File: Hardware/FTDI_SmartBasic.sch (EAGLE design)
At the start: 28 parts, among them U1 FT232RLSSOP, U2 MIC5219 3.3V, U3 TS3USB221A

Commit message: Incorporate changes from review
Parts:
- LOGO2: value SFE_LOGO_NAME_FLAME.1_INCH -> SFE_LOGO_FLAME.2_INCH; device SparkFun-Aesthetics:SFE_LOGO_NAME_FLAME.1_INCH -> SparkFun-Aesthetics:SFE_LOGO_FLAME.2_INCH
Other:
- note added: "01"
- note added: "Mike Hord"
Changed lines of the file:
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@@
 <part name="U$1" library="SparkFun-Aesthetics" deviceset="SMART_BASIC_LOGO" device=""/>
 <part name="LOGO1" library="SparkFun-Aesthetics" deviceset="SFE_LOGO_NAME" device=".1_INCH"/>
-<part name="LOGO2" library="SparkFun-Aesthetics" deviceset="SFE_LOGO_NAME_FLAME" device=".1_INCH"/>
 <part name="LOGO3" library="SparkFun-Aesthetics" deviceset="OSHW-LOGO" device="S"/>
+<part name="LOGO2" library="SparkFun-Aesthetics" deviceset="SFE_LOGO_FLAME" device=".2_INCH" value="SFE_LOGO_FLAME.2_INCH"/>
 </parts>
 <sheets>
@@
 Pro Mini,
 LilyPad, etc.</text>
+<text x="167.64" y="7.62" size="3.81" layer="91" font="vector">Mike Hord</text>
+<text x="239.014" y="6.604" size="3.81" layer="91" font="vector">01</text>
 </plain>
 <instances>
@@
 <instance part="U$1" gate="G$1" x="215.9" y="38.1"/>
 <instance part="LOGO1" gate="G$1" x="87.63" y="3.048"/>
-<instance part="LOGO2" gate="G$1" x="88.9" y="2.54"/>
 <instance part="LOGO3" gate="G$1" x="76.2" y="12.7"/>
+<instance part="LOGO2" gate="G$1" x="132.08" y="22.86"/>
 </instances>
 <busses>

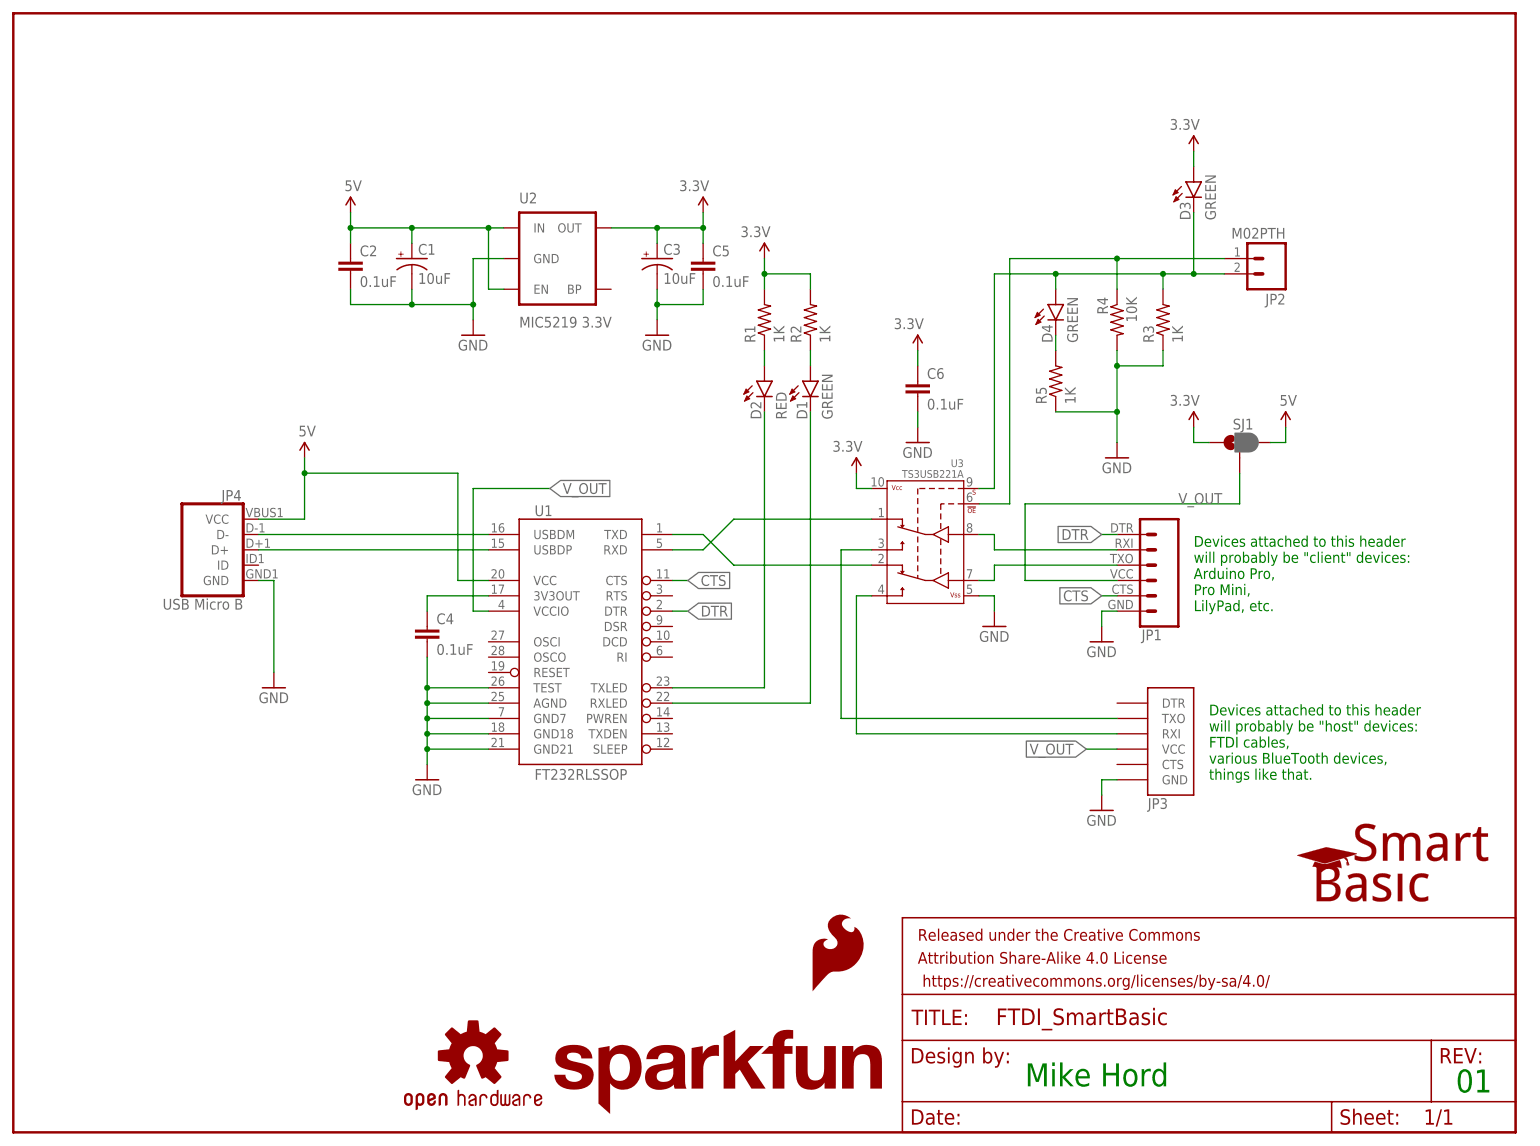
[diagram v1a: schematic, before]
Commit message: 2nd round protos - add vias to strain relief pads on connector - flip the client connector - remove the USB indicator LED and change other LED label - change silk from JP1 and JP3 to HOST and CLIENT
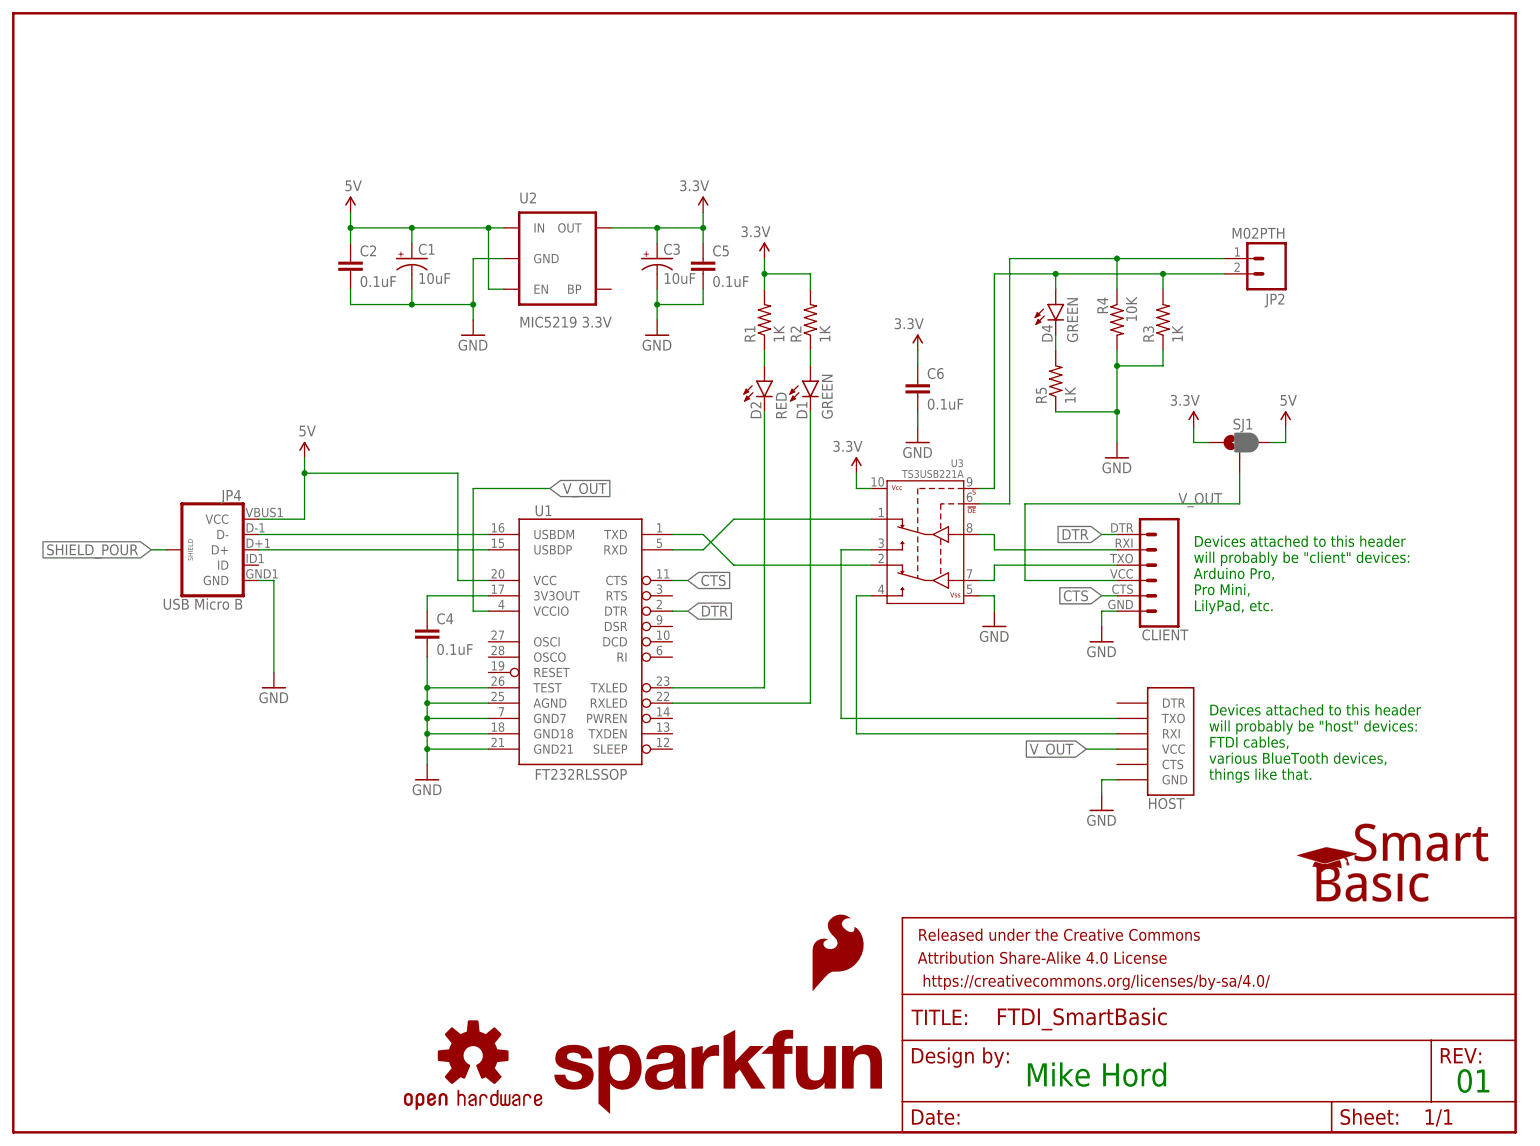
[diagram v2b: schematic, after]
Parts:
- removed D3: GREEN, SparkFun-LED:LED-GREEN0603
- renumbered JP1 to CLIENT, JP3 to HOST
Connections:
- new net SHIELD_POUR: JP4.SHIELD
- net 3.3V: no longer D3.A
- net SELECT: no longer D3.C
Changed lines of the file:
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@@
 <part name="GND1" library="SparkFun-Aesthetics" deviceset="GND" device=""/>
 <part name="SUPPLY4" library="SparkFun-Aesthetics" deviceset="5V" device=""/>
-<part name="JP1" library="SparkFun-Connectors" deviceset="FTDI_BASIC" device="PTH" value=""/>
+<part name="CLIENT" library="SparkFun-Connectors" deviceset="FTDI_BASIC" device="PTH" value=""/>
 <part name="R1" library="SparkFun-Resistors" deviceset="1KOHM1/10W1%(0603)" device="" value="1K"/>
 <part name="R2" library="SparkFun-Resistors" deviceset="1KOHM1/10W1%(0603)" device="" value="1K"/>
@@
 <part name="C3" library="SparkFun-Capacitors" deviceset="10UF-16V-10%(TANT)" device="" value="10uF"/>
 <part name="U3" library="SparkFun-AnalogIC" deviceset="TS3USB221A" device="" value="TS3USB221A"/>
-<part name="JP3" library="SparkFun-Connectors" deviceset="FTDI_DEVICE" device="" value=""/>
+<part name="HOST" library="SparkFun-Connectors" deviceset="FTDI_DEVICE" device="" value=""/>
 <part name="JP4" library="SparkFun-Connectors" deviceset="USB_MICROB_PLUG" device="CONN-11752" value="USB Micro B"/>
 <part name="SUPPLY6" library="SparkFun-Aesthetics" deviceset="3.3V" device=""/>
@@
 <part name="SUPPLY2" library="SparkFun-Aesthetics" deviceset="3.3V" device=""/>
 <part name="R3" library="SparkFun-Resistors" deviceset="1KOHM1/10W1%(0603)" device="" value="1K"/>
-<part name="D3" library="SparkFun-LED" deviceset="LED-GREEN" device="0603" value="GREEN"/>
-<part name="SUPPLY5" library="SparkFun-Aesthetics" deviceset="3.3V" device=""/>
 <part name="D4" library="SparkFun-LED" deviceset="LED-GREEN" device="0603" value="GREEN"/>
 <part name="R5" library="SparkFun-Resistors" deviceset="1KOHM1/10W1%(0603)" device="" value="1K"/>
@@
 <instance part="GND1" gate="1" x="43.18" y="73.66"/>
 <instance part="SUPPLY4" gate="G$1" x="48.26" y="111.76"/>
-<instance part="JP1" gate="G$1" x="187.96" y="93.98" smashed="yes" rot="R180">
+<instance part="CLIENT" gate="G$1" x="187.96" y="93.98" smashed="yes" rot="R180">
 <attribute name="VALUE" x="193.04" y="104.14" size="1.778" layer="96" rot="R180"/>
 <attribute name="NAME" x="186.944" y="81.534" size="1.778" layer="95"/>
@@
 <instance part="C3" gate="G$1" x="106.68" y="144.78"/>
 <instance part="U3" gate="G$1" x="157.48" y="88.9" rot="MR0"/>
-<instance part="JP3" gate="G$1" x="187.96" y="66.04" smashed="yes">
+<instance part="HOST" gate="G$1" x="187.96" y="66.04" smashed="yes">
 <attribute name="NAME" x="187.96" y="53.594" size="1.778" layer="95"/>
 <attribute name="VALUE" x="187.96" y="73.66" size="1.778" layer="96"/>
@@
 <instance part="SUPPLY2" gate="G$1" x="124.46" y="144.78" rot="MR0"/>
 <instance part="R3" gate="G$1" x="190.5" y="134.62" rot="R90"/>
-<instance part="D3" gate="G$1" x="195.58" y="157.48" smashed="yes">
-<attribute name="NAME" x="195.072" y="151.13" size="1.778" layer="95" rot="R90"/>
-<attribute name="VALUE" x="199.263" y="151.13" size="1.778" layer="96" rot="R90"/>
-</instance>
-<instance part="SUPPLY5" gate="G$1" x="195.58" y="162.56" rot="MR0"/>
 <instance part="D4" gate="G$1" x="172.72" y="137.16" smashed="yes">
 <attribute name="NAME" x="172.212" y="130.81" size="1.778" layer="95" rot="R90"/>
@@
 <pinref part="GND4" gate="1" pin="GND"/>
 <wire x1="180.34" y1="83.82" x2="180.34" y2="86.36" width="0.1524" layer="91"/>
-<pinref part="JP1" gate="G$1" pin="6"/>
+<pinref part="CLIENT" gate="G$1" pin="6"/>
 <wire x1="180.34" y1="86.36" x2="182.88" y2="86.36" width="0.1524" layer="91"/>
 </segment>
@@
 </segment>
 <segment>
-<pinref part="JP3" gate="G$1" pin="GND"/>
+<pinref part="HOST" gate="G$1" pin="GND"/>
 <pinref part="GND8" gate="1" pin="GND"/>
 <wire x1="182.88" y1="58.42" x2="180.34" y2="58.42" width="0.1524" layer="91"/>
@@
 </segment>
 <segment>
-<pinref part="D3" gate="G$1" pin="A"/>
-<wire x1="195.58" y1="160.02" x2="195.58" y2="162.56" width="0.1524" layer="91"/>
-<pinref part="SUPPLY5" gate="G$1" pin="3.3V"/>
-</segment>
-<segment>
 <pinref part="C6" gate="G$1" pin="1"/>
 <pinref part="SUPPLY9" gate="G$1" pin="3.3V"/>
@@
 <wire x1="162.56" y1="106.68" x2="160.02" y2="106.68" width="0.1524" layer="91"/>
 <pinref part="JP2" gate="G$1" pin="2"/>
-<wire x1="190.5" y1="142.24" x2="195.58" y2="142.24" width="0.1524" layer="91"/>
 <pinref part="R3" gate="G$1" pin="2"/>
-<pinref part="D3" gate="G$1" pin="C"/>
-<wire x1="195.58" y1="142.24" x2="200.66" y2="142.24" width="0.1524" layer="91"/>
-<wire x1="195.58" y1="152.4" x2="195.58" y2="142.24" width="0.1524" layer="91"/>
-<junction x="195.58" y="142.24"/>
+<wire x1="190.5" y1="142.24" x2="200.66" y2="142.24" width="0.1524" layer="91"/>
 <pinref part="D4" gate="G$1" pin="A"/>
 <wire x1="172.72" y1="142.24" x2="172.72" y2="139.7" width="0.1524" layer="91"/>
@@
 <net name="N$13" class="0">
 <segment>
-<pinref part="JP1" gate="G$1" pin="2"/>
+<pinref part="CLIENT" gate="G$1" pin="2"/>
 <wire x1="182.88" y1="96.52" x2="162.56" y2="96.52" width="0.1524" layer="91"/>
 <wire x1="162.56" y1="96.52" x2="162.56" y2="99.06" width="0.1524" layer="91"/>
@@
 <net name="N$14" class="0">
 <segment>
-<pinref part="JP1" gate="G$1" pin="3"/>
+<pinref part="CLIENT" gate="G$1" pin="3"/>
 <wire x1="182.88" y1="93.98" x2="162.56" y2="93.98" width="0.1524" layer="91"/>
 <wire x1="162.56" y1="93.98" x2="162.56" y2="91.44" width="0.1524" layer="91"/>
@@
 <net name="V_OUT" class="0">
 <segment>
-<pinref part="JP1" gate="G$1" pin="4"/>
+<pinref part="CLIENT" gate="G$1" pin="4"/>
 <wire x1="182.88" y1="91.44" x2="167.64" y2="91.44" width="0.1524" layer="91"/>
 <wire x1="167.64" y1="91.44" x2="167.64" y2="104.14" width="0.1524" layer="91"/>
@@
 </segment>
 <segment>
-<pinref part="JP3" gate="G$1" pin="VCC"/>
+<pinref part="HOST" gate="G$1" pin="VCC"/>
 <wire x1="182.88" y1="63.5" x2="177.8" y2="63.5" width="0.1524" layer="91"/>
 <label x="177.8" y="63.5" size="1.778" layer="95" rot="R180" xref="yes"/>
@@
 <wire x1="142.24" y1="96.52" x2="137.16" y2="96.52" width="0.1524" layer="91"/>
 <wire x1="137.16" y1="96.52" x2="137.16" y2="68.58" width="0.1524" layer="91"/>
-<pinref part="JP3" gate="G$1" pin="TXO"/>
+<pinref part="HOST" gate="G$1" pin="TXO"/>
 <wire x1="137.16" y1="68.58" x2="182.88" y2="68.58" width="0.1524" layer="91"/>
 </segment>
@@
 <wire x1="142.24" y1="88.9" x2="139.7" y2="88.9" width="0.1524" layer="91"/>
 <wire x1="139.7" y1="88.9" x2="139.7" y2="66.04" width="0.1524" layer="91"/>
-<pinref part="JP3" gate="G$1" pin="RXI"/>
+<pinref part="HOST" gate="G$1" pin="RXI"/>
 <wire x1="139.7" y1="66.04" x2="182.88" y2="66.04" width="0.1524" layer="91"/>
 </segment>
@@
 </segment>
 <segment>
-<pinref part="JP1" gate="G$1" pin="5"/>
+<pinref part="CLIENT" gate="G$1" pin="5"/>
 <wire x1="182.88" y1="88.9" x2="180.34" y2="88.9" width="0.1524" layer="91"/>
 <label x="180.34" y="88.9" size="1.778" layer="95" rot="R180" xref="yes"/>
@@
 </segment>
 <segment>
-<pinref part="JP1" gate="G$1" pin="1"/>
+<pinref part="CLIENT" gate="G$1" pin="1"/>
 <wire x1="182.88" y1="99.06" x2="180.34" y2="99.06" width="0.1524" layer="91"/>
 <label x="180.34" y="99.06" size="1.778" layer="95" rot="R180" xref="yes"/>
@@
 </segment>
 </net>
+<net name="SHIELD_POUR" class="0">
+<segment>
+<pinref part="JP4" gate="G$1" pin="SHIELD"/>
+<wire x1="25.4" y1="96.52" x2="22.86" y2="96.52" width="0.1524" layer="91"/>
+<label x="22.86" y="96.52" size="1.778" layer="95" rot="R180" xref="yes"/>
+</segment>
+</net>

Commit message: Minor changes from review
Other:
- note added: "02"
- note removed: "01"
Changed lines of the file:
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@@
 LilyPad, etc.</text>
 <text x="167.64" y="7.62" size="3.81" layer="91" font="vector">Mike Hord</text>
-<text x="239.014" y="6.604" size="3.81" layer="91" font="vector">01</text>
+<text x="239.014" y="6.604" size="3.81" layer="91" font="vector">02</text>
 </plain>
 <instances>

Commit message: Ready for review for reds
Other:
- note added: "10.0"
- note removed: "02"
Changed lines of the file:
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@@
 LilyPad, etc.</text>
 <text x="167.64" y="7.62" size="3.81" layer="91" font="vector">Mike Hord</text>
-<text x="239.014" y="6.604" size="3.81" layer="91" font="vector">02</text>
+<text x="236.22" y="6.35" size="3.81" layer="91" font="vector">10.0</text>
 </plain>
 <instances>

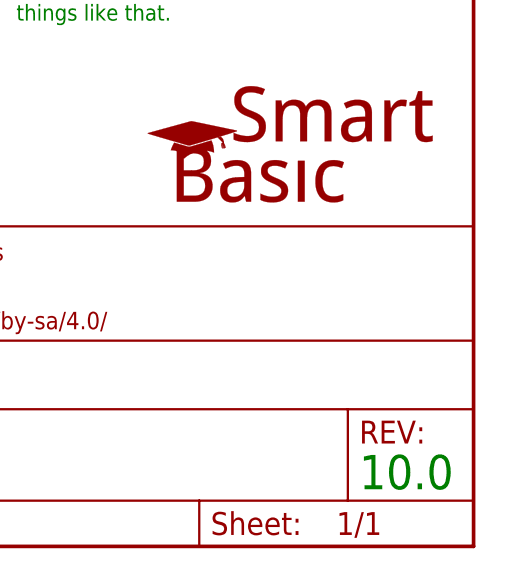
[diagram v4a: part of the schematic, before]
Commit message: added local fiducials
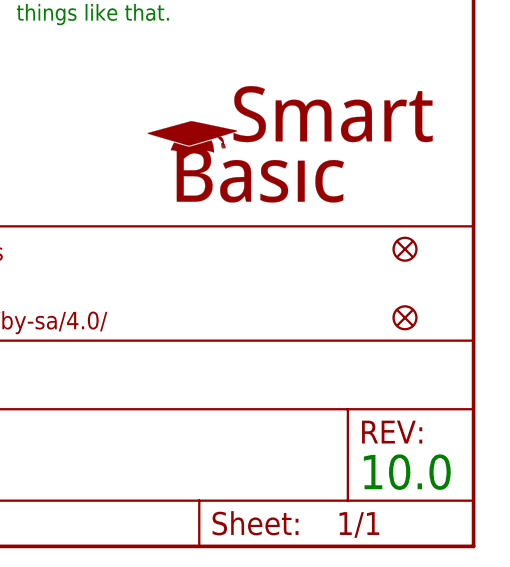
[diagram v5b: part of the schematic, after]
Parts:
- added FID1, FID2: FIDUCIAL1X2, SparkFun-Aesthetics:FIDUCIAL1X2
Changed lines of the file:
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@@
 <?xml version="1.0" encoding="utf-8"?>
 <!DOCTYPE eagle SYSTEM "eagle.dtd">
-<eagle version="6.5.0">
+<eagle version="6.6.0">
 <drawing>
 <settings>
@@
 <part name="LOGO3" library="SparkFun-Aesthetics" deviceset="OSHW-LOGO" device="S"/>
 <part name="LOGO2" library="SparkFun-Aesthetics" deviceset="SFE_LOGO_FLAME" device=".2_INCH" value="SFE_LOGO_FLAME.2_INCH"/>
+<part name="FID1" library="SparkFun-Aesthetics" deviceset="FIDUCIAL" device="1X2"/>
+<part name="FID2" library="SparkFun-Aesthetics" deviceset="FIDUCIAL" device="1X2"/>
 </parts>
 <sheets>
@@
 <instance part="LOGO3" gate="G$1" x="76.2" y="12.7"/>
 <instance part="LOGO2" gate="G$1" x="132.08" y="22.86"/>
+<instance part="FID1" gate="G$1" x="241.3" y="33.02"/>
+<instance part="FID2" gate="G$1" x="241.3" y="25.4"/>
 </instances>
 <busses>

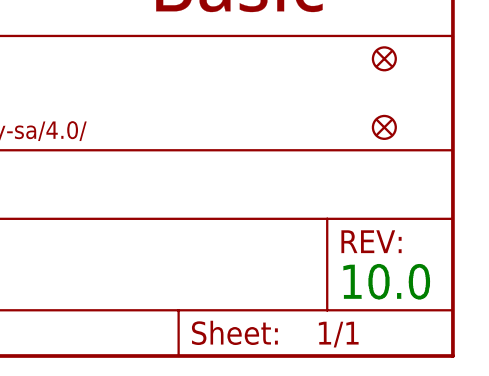
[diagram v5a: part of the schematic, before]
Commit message: Fixed bottom silk, rev to 11
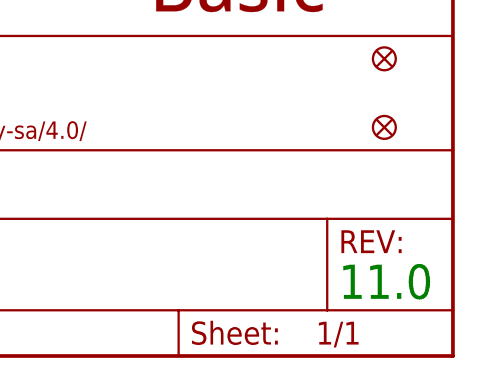
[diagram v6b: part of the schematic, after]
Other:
- note added: "11.0"
- note removed: "10.0"
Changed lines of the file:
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@@
 <?xml version="1.0" encoding="utf-8"?>
 <!DOCTYPE eagle SYSTEM "eagle.dtd">
-<eagle version="6.6.0">
+<eagle version="6.5.0">
 <drawing>
 <settings>
@@
 <layer number="254" name="cooling" color="7" fill="1" visible="yes" active="yes"/>
 </layers>
-<schematic xreflabel="%F%N/%S.%C%R" xrefpart="1_/%S.%C%R">
+<schematic xreflabel="%F%N/%S" xrefpart="1_/%S.%C%R">
 <attributes>
 </attributes>
@@
 LilyPad, etc.</text>
 <text x="167.64" y="7.62" size="3.81" layer="91" font="vector">Mike Hord</text>
-<text x="236.22" y="6.35" size="3.81" layer="91" font="vector">10.0</text>
+<text x="236.22" y="6.35" size="3.81" layer="91" font="vector">11.0</text>
 </plain>
 <instances>
